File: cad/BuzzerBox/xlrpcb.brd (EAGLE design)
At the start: 115.6 x 164.6 mm, 11 parts, among them X1 NC3, X10 NC3, X12 87758-2616, X2 NC3, X3 NC3, X4 NC3, X5 NC3, X6 NC3, X7 NC3, X8 NC3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

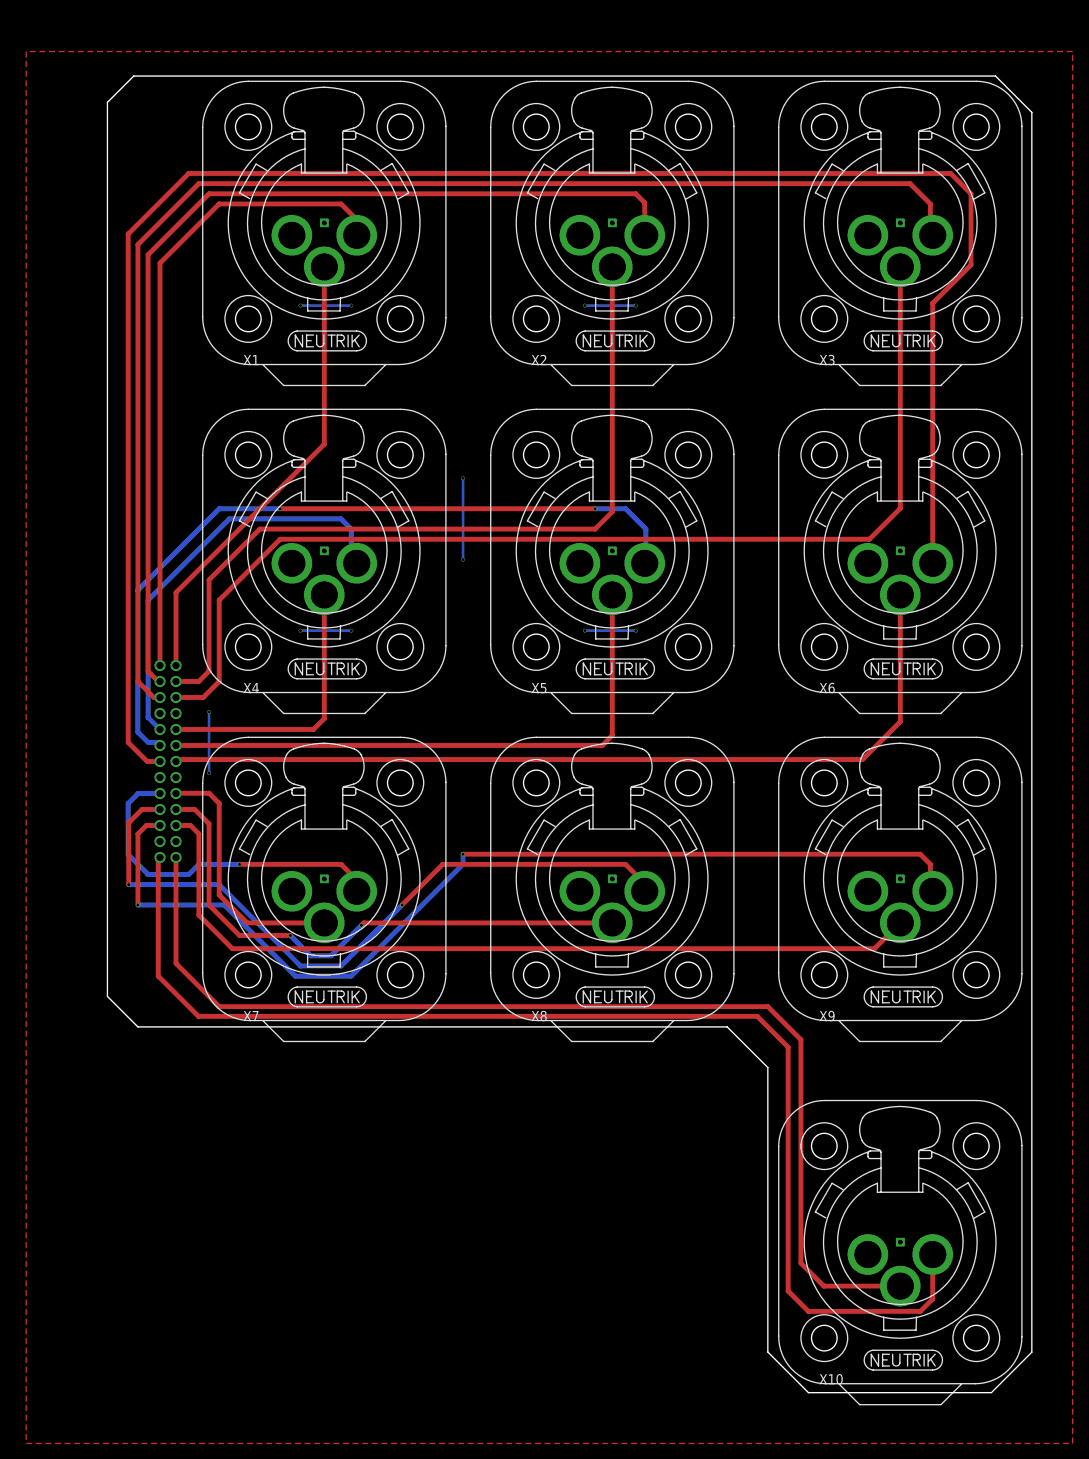
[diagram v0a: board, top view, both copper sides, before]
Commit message: Changed keepout etc for xlr connectors.
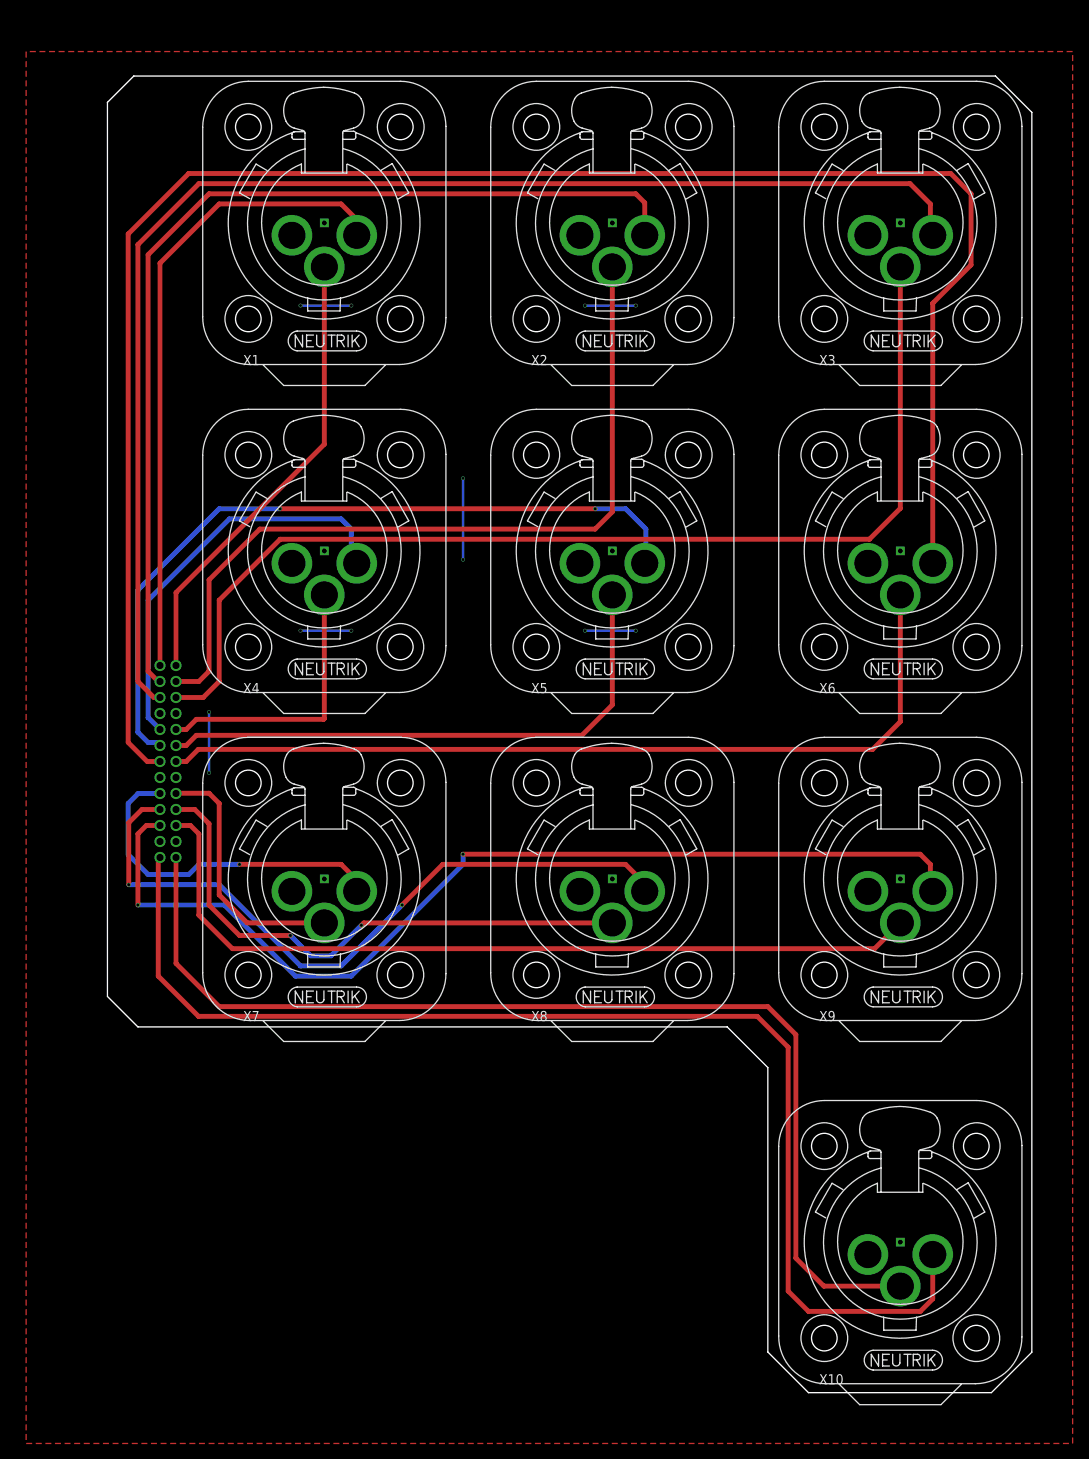
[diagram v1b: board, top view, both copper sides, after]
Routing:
- net BUZZ5: track 72.6 -> 70.4 mm

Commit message: Change XLR PCB to equal spacing
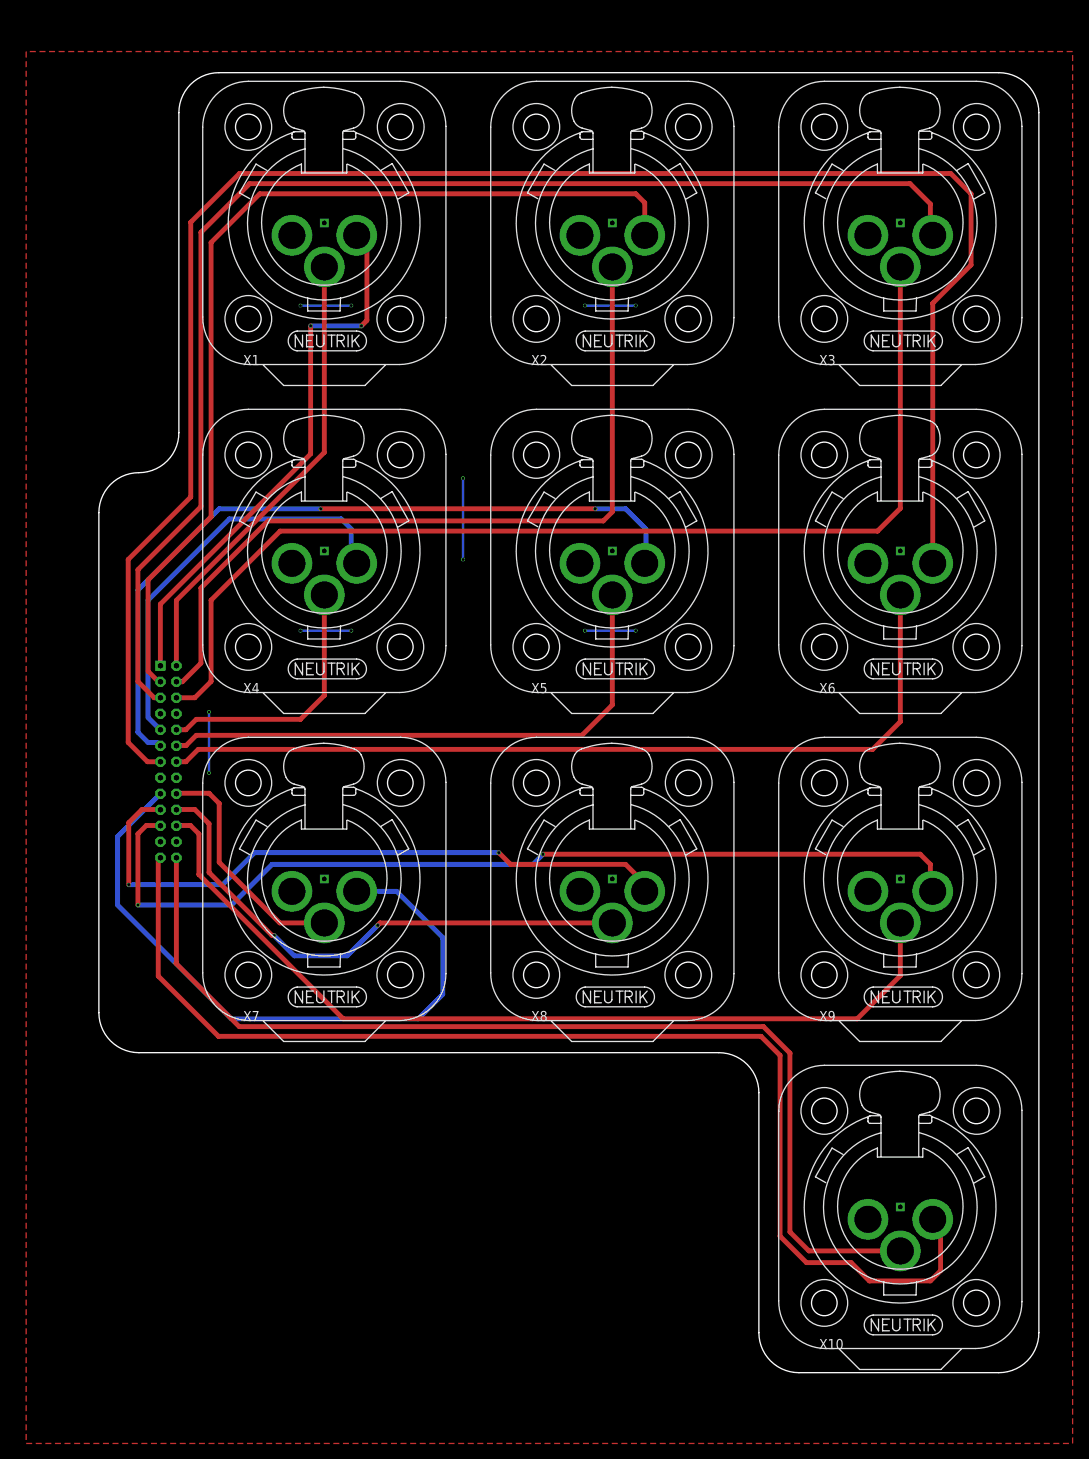
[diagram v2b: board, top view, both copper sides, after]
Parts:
- removed X12: 87758-2616, con-molex:87758-2616
- added X11: B26B-PHDSS, con-JST PHD:B26B-PHDSS
- moved X10 4.40 mm to (87.7, 23.2)
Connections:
- net BUZZ0: now also X11.26; no longer X12.25
- net BUZZ1: now also X11.2; no longer X12.1
- net BUZZ2: now also X11.4; no longer X12.3
- net BUZZ3: now also X11.6; no longer X12.5
- net BUZZ4: now also X11.10; no longer X12.9
- net BUZZ5: now also X11.12; no longer X12.11
- net BUZZ6: now also X11.14; no longer X12.13
- net BUZZ7: now also X11.18; no longer X12.17
- net BUZZ8: now also X11.20; no longer X12.19
- net BUZZ9: now also X11.22; no longer X12.21
- net GND: now also X11.15, X11.16, X11.23, X11.24, X11.7, X11.8; no longer X12.15, X12.16, X12.23, X12.24, X12.7, X12.8
- net LED0: now also X11.25; no longer X12.26
- net LED1: now also X11.1; no longer X12.2
- net LED2: now also X11.3; no longer X12.4
- net LED3: now also X11.5; no longer X12.6
- net LED4: now also X11.9; no longer X12.10
- net LED5: now also X11.11; no longer X12.12
- net LED6: now also X11.13; no longer X12.14
- net LED7: now also X11.17; no longer X12.18
- net LED8: now also X11.19; no longer X12.20
- net LED9: now also X11.21; no longer X12.22
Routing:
- net LED7: track 43.2 -> 84.2 mm, vias 1 -> 0
- net LED1: track 80.7 -> 68.7 mm, vias 0 -> 2
- net BUZZ9: track 104.2 -> 112.3 mm
- net LED9: track 125.9 -> 117.9 mm
- net LED8: track 88.3 -> 81.1 mm
- net BUZZ0: track 136.9 -> 131.7 mm
- net LED0: track 153.1 -> 149.1 mm
- net LED6: track 226.2 -> 222.6 mm
- net LED3: track 165.5 -> 161.9 mm
- net LED2: track 123.9 -> 120.2 mm
- net BUZZ8: track 69.8 -> 67.4 mm
- net BUZZ7: track 32.0 -> 29.5 mm
- net BUZZ4: track 34.6 -> 32.8 mm
- net BUZZ2: track 100.6 -> 99.4 mm
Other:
- board size 115.6 x 164.6 mm -> 117.5 x 162.5 mm
- board text added: "XLR-TOP-Board v2"
- board text removed: "XLR-TOP-Board v1"

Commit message: Added PE to XLR Board
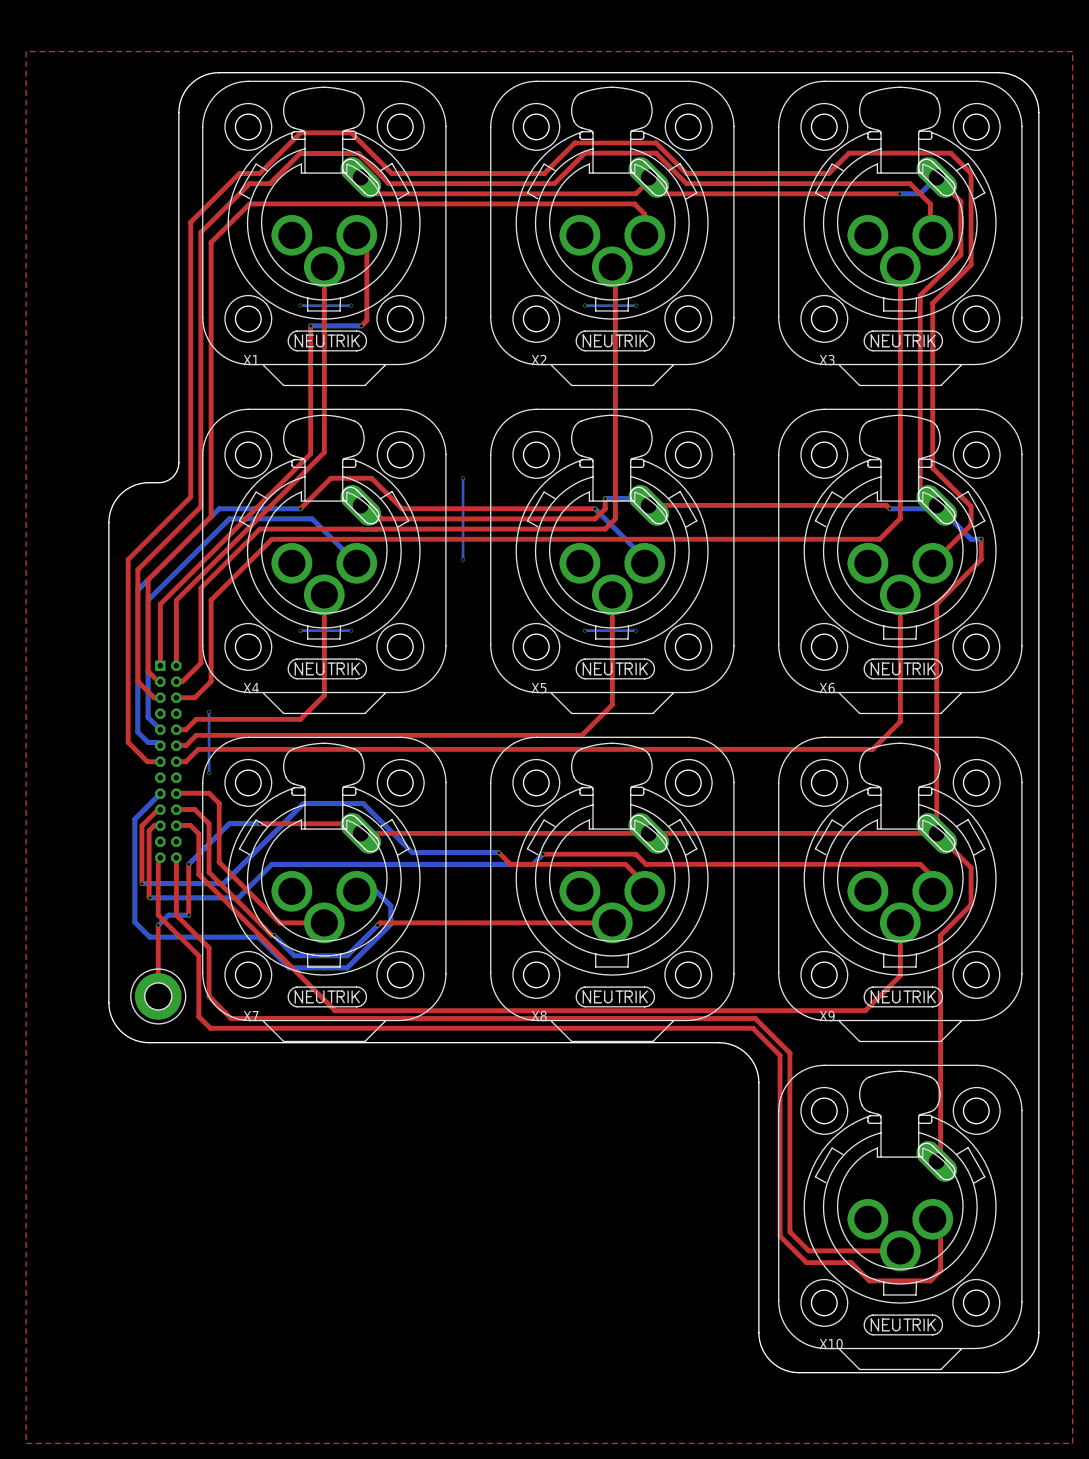
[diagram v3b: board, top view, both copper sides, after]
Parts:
- added H1: MOUNT-PAD-ROUND3.2, holes:3,2-PAD
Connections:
- new net PE: H1.B3,2, X1.P$4, X10.P$4, X2.P$4, X3.P$4, X4.P$4, X5.P$4, X6.P$4, X7.P$4, X8.P$4, X9.P$4
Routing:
- net PE: track 0.00 -> 402.7 mm, vias 0 -> 8
- net LED7: track 84.2 -> 61.3 mm
- net LED6: track 222.6 -> 237.5 mm
- net LED3: track 161.9 -> 168.2 mm
- net LED9: track 117.9 -> 113.2 mm
- net LED4: track 51.5 -> 49.4 mm
- net LED2: track 120.2 -> 118.3 mm
- net LED8: track 81.1 -> 82.5 mm
- net BUZZ2: track 99.4 -> 100.5 mm
- net LED5: track 94.4 -> 95.3 mm
- net BUZZ9: track 112.3 -> 111.5 mm
- net BUZZ3: track 136.4 -> 137.2 mm
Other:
- board size 117.5 x 162.5 mm -> 116.2 x 162.5 mm

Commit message: V3 XLRBoard
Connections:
- net BUZZ0: now also X10.P$1; no longer X10.P$2
- net BUZZ1: now also X1.P$1; no longer X1.P$2
- net BUZZ2: now also X2.P$1; no longer X2.P$2
- net BUZZ3: now also X3.P$1; no longer X3.P$2
- net BUZZ4: now also X4.P$1; no longer X4.P$2
- net BUZZ5: now also X5.P$1; no longer X5.P$2
- net BUZZ6: now also X6.P$1; no longer X6.P$2
- net BUZZ7: now also X7.P$1; no longer X7.P$2
- net BUZZ8: now also X8.P$1; no longer X8.P$2
- net BUZZ9: now also X9.P$1; no longer X9.P$2
- net GND: now also X1.P$3, X10.P$3, X2.P$3, X3.P$3, X4.P$3, X5.P$3, X6.P$3, X7.P$3, X8.P$3, X9.P$3; no longer X1.P$1, X10.P$1, X2.P$1, X3.P$1, X4.P$1, X5.P$1, X6.P$1, X7.P$1, X8.P$1, X9.P$1
- net LED0: now also X10.P$2; no longer X10.P$3
- net LED1: now also X1.P$2; no longer X1.P$3
- net LED2: now also X2.P$2; no longer X2.P$3
- net LED3: now also X3.P$2; no longer X3.P$3
- net LED4: now also X4.P$2; no longer X4.P$3
- net LED5: now also X5.P$2; no longer X5.P$3
- net LED6: now also X6.P$2; no longer X6.P$3
- net LED7: now also X7.P$2; no longer X7.P$3
- net LED8: now also X8.P$2; no longer X8.P$3
- net LED9: now also X9.P$2; no longer X9.P$3
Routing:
- net PE: track 402.7 -> 0.00 mm, vias 8 -> 0
- net GND: track 43.2 -> 74.7 mm, vias 12 -> 18
- net LED7: track 61.3 -> 42.6 mm
- net LED0: track 149.1 -> 134.5 mm
- net LED6: track 237.5 -> 249.1 mm
- net LED1: track 68.7 -> 58.3 mm, vias 2 -> 0
- net BUZZ3: track 137.2 -> 146.0 mm
- net BUZZ0: track 131.7 -> 123.9 mm
- net BUZZ2: track 100.5 -> 108.2 mm, vias 0 -> 2
- net BUZZ7: track 29.5 -> 23.9 mm
- net BUZZ1: track 57.5 -> 62.9 mm, vias 0 -> 2
- net BUZZ8: track 67.4 -> 64.6 mm, vias 2 -> 0
- net BUZZ4: track 32.8 -> 30.3 mm
- net LED5: track 95.3 -> 97.5 mm
- net LED9: track 113.2 -> 115.0 mm
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- added copper zone on layer 16, net PE
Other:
- board text added: "XLR-TOP-Board v3"
- board text removed: "XLR-TOP-Board v2"
